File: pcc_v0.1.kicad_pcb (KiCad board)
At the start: 2 copper layers, 170.3 x 151.7 mm, 65 parts, among them J2 Conn_01x04_Socket, J3 Conn_01x02_Socket, J4 Conn_02x14_Counter_Clockwise, J6 Conn_01x04_Socket, J7 Conn_01x04_Socket, J8 Conn_01x02_Socket, K1 G9KB-1A_DC12, K2 DBR71210, K3 PCN-112D3MHZ_000, U2 4N35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

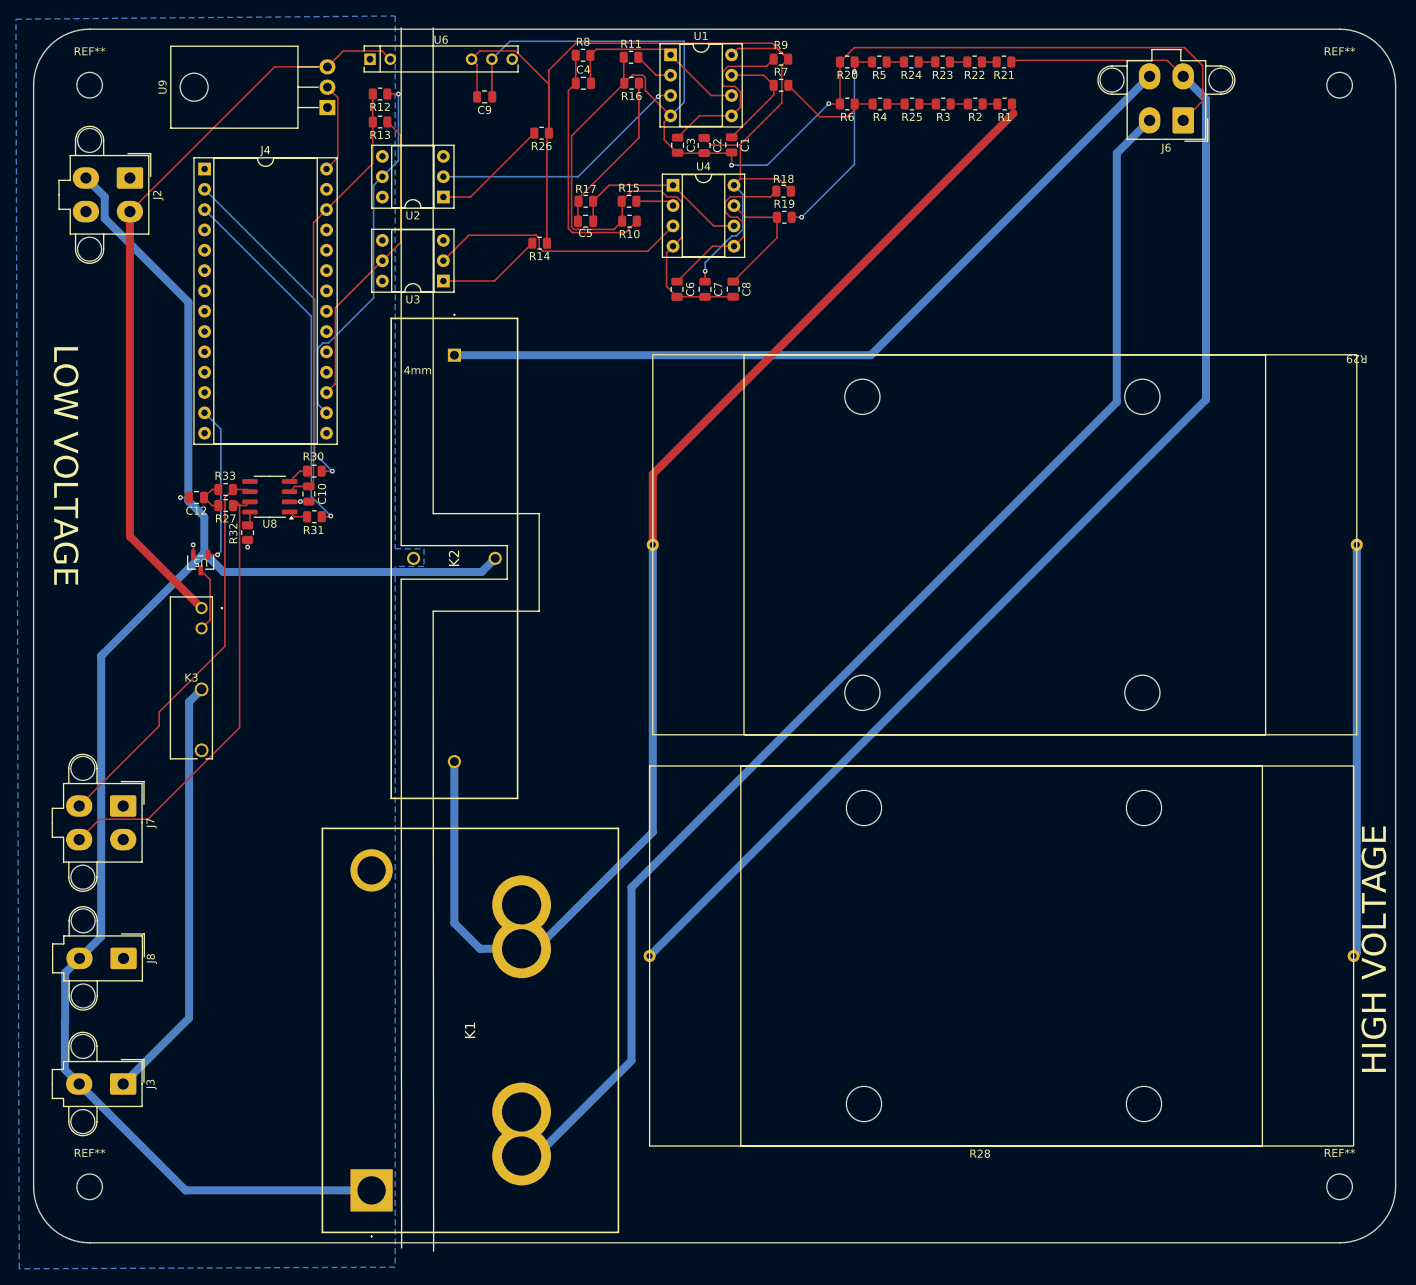
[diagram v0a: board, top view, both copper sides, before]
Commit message: made custom footprint for relay. need to measure actual size
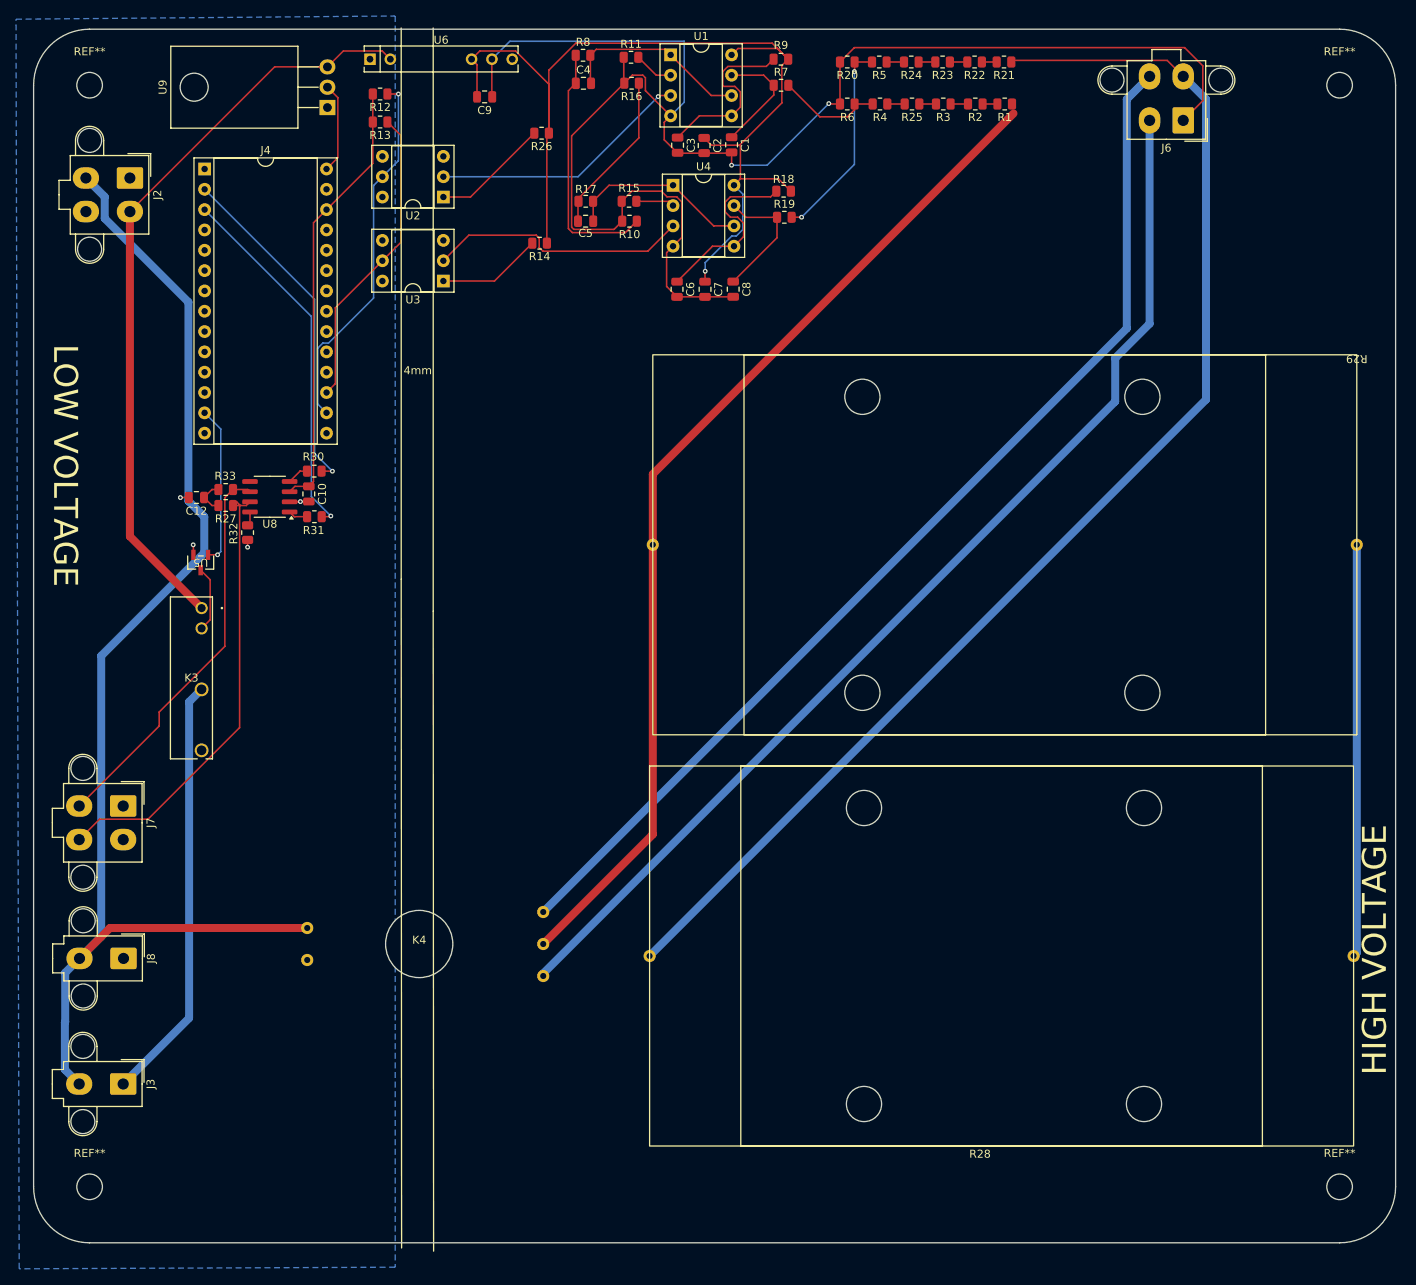
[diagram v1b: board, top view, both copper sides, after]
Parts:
- removed K1: G9KB-1A_DC12, precharge relay 2:G9KB1ADC12
- removed K2: DBR71210, discharge relay:DBR71210
- added K4: Relay_SPDT, Relay_THT:Precharge_Discharge_Relay, F.Cu at (101.0, 135.0)
- C10: value 100nF -> 100n
- C12: value 4.7nF -> 4.7n
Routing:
- net Shutdown_in: track 207.5 -> 157.4 mm
- net TS+: track 101.3 -> 135.8 mm
- net Vin_Accu: track 160.9 -> 128.2 mm
- net B+_in: track 163.0 -> 138.3 mm

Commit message: corrected relay footprint, added flyback diode
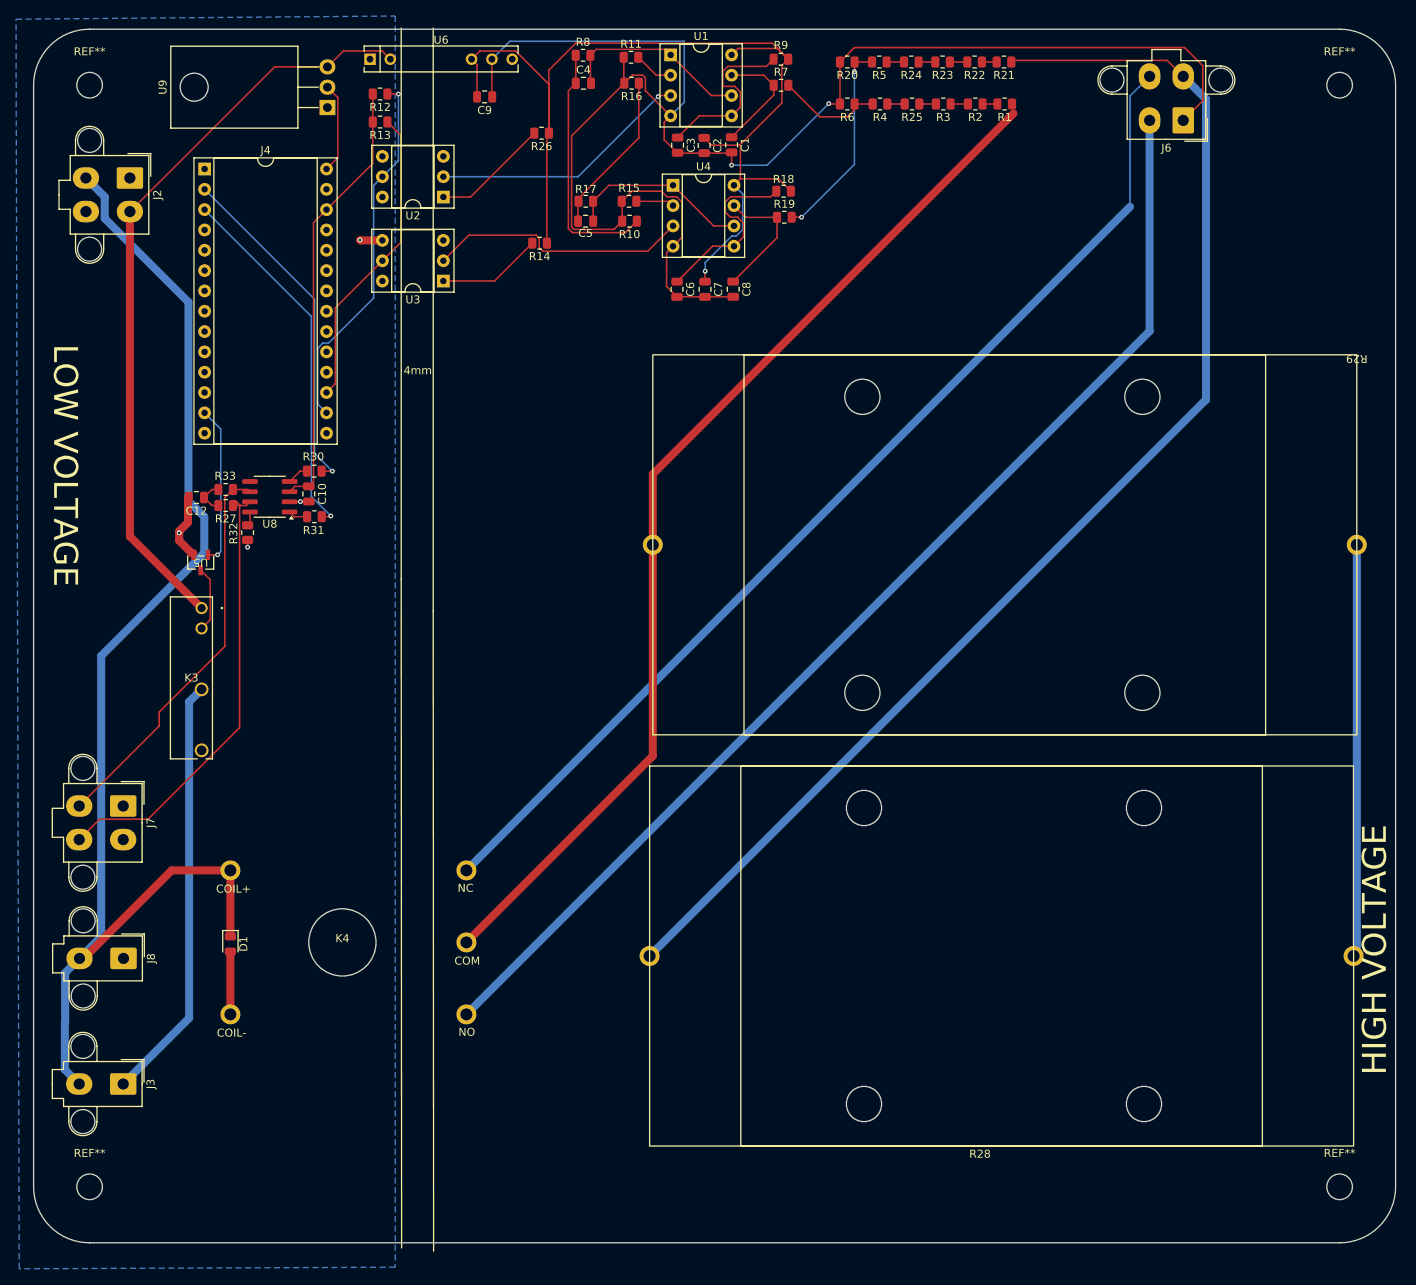
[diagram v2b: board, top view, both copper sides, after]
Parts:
- added D1: D, Diode_SMD:D_0805_2012Metric, F.Cu at (77.4, 135.0)
- moved K4 9.60 mm to (91.4, 134.8)
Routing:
- net GLV-: track 5.64 -> 22.2 mm
- net B+_in: track 138.3 -> 147.1 mm
- net Vin_Accu: track 128.2 -> 131.9 mm
- net Shutdown_in: track 157.4 -> 158.9 mm
- net TS+: track 135.8 -> 134.6 mm

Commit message: changed diode to tht and added connector labels
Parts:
- D1: footprint Diode_SMD:D_0805_2012Metric -> Diode_THT:D_5KPW_P7.62mm_Vertical_AnodeUp
- moved D1 3.80 mm to (77.4, 131.2)
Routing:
- net GLV-: track 22.2 -> 14.4 mm
- net Shutdown_in: track 158.9 -> 156.2 mm
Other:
- board text added: "CAN Bus"
- board text added: "HV IN"
- board text added: "IR+ Relay"
- board text added: "IR- Relay"
- board text added: "POWER IN"
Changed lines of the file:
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@@
 		)
 	)
-	(footprint "Diode_SMD:D_0805_2012Metric"
+	(footprint "Diode_THT:D_5KPW_P7.62mm_Vertical_AnodeUp"
 		(layer "F.Cu")
-		(at 77.4 135 -90)
-		(descr "Diode SMD 0805 (2012 Metric), square (rectangular) end terminal, IPC_7351 nominal, (Body size source: https://docs.google.com/spreadsheets/d/1BsfQQcO9C6DZCsRaXUlFlo91Tg2WpOkGARC1WS5S8t0/edit?usp=sharing), generated with kicad-footprint-generator")
-		(tags "diode")
+		(at 77.4 131.2 -90)
+		(descr "Diode, 5KPW series, Axial, Vertical, pin pitch=7.62mm, , length*diameter=9*8mm^2, , http://www.diodes.com/_files/packages/8686949.gif")
+		(tags "Diode 5KPW series Axial Vertical pin pitch 7.62mm  length 9mm diameter 8mm")
 		(property "Reference" "D1"
-			(at 0 -1.65 90)
+			(at 3.81 -5.12 -90)
 			(layer "F.SilkS")
 			(effects
@@
 		)
 		(property "Value" "D"
-			(at 0 1.65 90)
+			(at 3.81 5.12 -90)
 			(layer "F.Fab")
 			(effects
@@
 			)
 		)
-		(property "Footprint" "Diode_SMD:D_0805_2012Metric"
+		(property "Footprint" "Diode_THT:D_5KPW_P7.62mm_Vertical_AnodeUp"
 			(at 0 0 -90)
 			(unlocked yes)
@@
 		(sheetname "Root")
 		(sheetfile "pcc_v0.1.kicad_sch")
-		(attr smd)
-		(fp_line
-			(start -1.685 0.96)
-			(end 1 0.96)
-			(stroke
-				(width 0.12)
-				(type solid)
-			)
-			(layer "F.SilkS")
-		)
+		(attr through_hole)
 		(fp_line
-			(start -1.685 -0.96)
-			(end -1.685 0.96)
+			(start 4.12 0)
+			(end 5.72 0)
 			(stroke
 				(width 0.12)
@@
 			(layer "F.SilkS")
 		)
-		(fp_line
-			(start 1 -0.96)
-			(end -1.685 -0.96)
+		(fp_circle
+			(center 0 0)
+			(end 4.12 0)
 			(stroke
 				(width 0.12)
 				(type solid)
 			)
+			(fill none)
 			(layer "F.SilkS")
 		)
 		(fp_line
-			(start -1.68 0.95)
-			(end -1.68 -0.95)
+			(start -4.25 4.25)
+			(end 9.47 4.25)
 			(stroke
 				(width 0.05)
@@
 		)
 		(fp_line
-			(start 1.68 0.95)
-			(end -1.68 0.95)
+			(start 9.47 4.25)
+			(end 9.47 -4.25)
 			(stroke
 				(width 0.05)
@@
 		)
 		(fp_line
-			(start -1.68 -0.95)
-			(end 1.68 -0.95)
+			(start -4.25 -4.25)
+			(end -4.25 4.25)
 			(stroke
 				(width 0.05)
@@
 		)
 		(fp_line
-			(start 1.68 -0.95)
-			(end 1.68 0.95)
+			(start 9.47 -4.25)
+			(end -4.25 -4.25)
 			(stroke
 				(width 0.05)
@@
 		)
 		(fp_line
-			(start -1 0.6)
-			(end 1 0.6)
+			(start 0 0)
+			(end 7.62 0)
 			(stroke
 				(width 0.1)
@@
 			(layer "F.Fab")
 		)
-		(fp_line
-			(start 1 0.6)
-			(end 1 -0.6)
+		(fp_circle
+			(center 0 0)
+			(end 4 0)
 			(stroke
 				(width 0.1)
 				(type solid)
 			)
+			(fill none)
 			(layer "F.Fab")
 		)
-		(fp_line
-			(start -1 -0.3)
-			(end -1 0.6)
-			(stroke
-				(width 0.1)
-				(type solid)
+		(fp_text user "A"
+			(at 7.62 2.6 -90)
+			(layer "F.SilkS")
+			(effects
+				(font
+					(size 1 1)
+					(thickness 0.15)
+				)
 			)
-			(layer "F.Fab")
 		)
-		(fp_line
-			(start -0.7 -0.6)
-			(end -1 -0.3)
-			(stroke
-				(width 0.1)
-				(type solid)
-			)
+		(fp_text user "${REFERENCE}"
+			(at 0 -2.1 -90)
 			(layer "F.Fab")
-		)
-		(fp_line
-			(start 1 -0.6)
-			(end -0.7 -0.6)
-			(stroke
-				(width 0.1)
-				(type solid)
+			(effects
+				(font
+					(size 1 1)
+					(thickness 0.15)
+				)
 			)
-			(layer "F.Fab")
 		)
-		(fp_text user "${REFERENCE}"
-			(at 0 0 90)
+		(fp_text user "A"
+			(at 7.62 2.6 -90)
 			(layer "F.Fab")
 			(effects
 				(font
-					(size 0.5 0.5)
-					(thickness 0.08)
+					(size 1 1)
+					(thickness 0.15)
 				)
 			)
 		)
-		(pad "1" smd roundrect
-			(at -0.9375 0 270)
-			(size 0.975 1.4)
-			(layers "F.Cu" "F.Paste" "F.Mask")
-			(roundrect_rratio 0.25)
+		(pad "1" thru_hole rect
+			(at 0 0 270)
+			(size 3.2 3.2)
+			(drill 1.6)
+			(layers "*.Cu" "*.Mask")
+			(remove_unused_layers no)
 			(net 69 "Shutdown_in")
 			(pinfunction "K")
 			(pintype "passive")
 		)
-		(pad "2" smd roundrect
-			(at 0.9375 0 270)
-			(size 0.975 1.4)
-			(layers "F.Cu" "F.Paste" "F.Mask")
-			(roundrect_rratio 0.25)
+		(pad "2" thru_hole oval
+			(at 7.62 0 270)
+			(size 3.2 3.2)
+			(drill 1.6)
+			(layers "*.Cu" "*.Mask")
+			(remove_unused_layers no)
 			(net 8 "GLV-")
 			(pinfunction "A")
 			(pintype "passive")
 		)
-		(model "${KICAD8_3DMODEL_DIR}/Diode_SMD.3dshapes/D_0805_2012Metric.wrl"
+		(model "${KICAD8_3DMODEL_DIR}/Diode_THT.3dshapes/D_5KPW_P7.62mm_Vertical_AnodeUp.wrl"
 			(offset
 				(xyz 0 0 0)
@@
 	)
 	(gr_line
-		(start 98.773804 129.199896)
-		(end 98.8 173)
-		(stroke
-			(width 0.1)
-			(type default)
-		)
-		(layer "F.SilkS")
-	)
-	(gr_line
 		(start 98.772608 127.200016)
 		(end 98.773804 129.199896)
@@
 		(layer "F.SilkS")
 	)
+	(gr_line
+		(start 98.773804 129.199896)
+		(end 98.8 173)
+		(stroke
+			(width 0.1)
+			(type default)
+		)
+		(layer "F.SilkS")
+	)
 	(gr_arc
 		(start 59.800253 172.350253)
@@
 		(layer "Edge.Cuts")
 	)
+	(gr_text "CAN Bus"
+		(at 70.2 125 90)
+		(layer "F.SilkS")
+		(effects
+			(font
+				(size 1.5 1.5)
+				(thickness 0.3)
+				(bold yes)
+			)
+			(justify left bottom)
+		)
+	)
+	(gr_text "HV IN"
+		(at 191.2 39 0)
+		(layer "F.SilkS")
+		(effects
+			(font
+				(size 1.5 1.5)
+				(thickness 0.3)
+				(bold yes)
+			)
+			(justify left bottom)
+		)
+	)
 	(gr_text "4mm"
 		(at 99.050253 63.900253 0)
@@
 		)
 	)
+	(gr_text "POWER IN"
+		(at 71.2 46.8 90)
+		(layer "F.SilkS")
+		(effects
+			(font
+				(size 1.5 1.5)
+				(thickness 0.3)
+				(bold yes)
+			)
+			(justify left bottom)
+		)
+	)
+	(gr_text "IR- Relay"
+		(at 70.2 142.4 90)
+		(layer "F.SilkS")
+		(effects
+			(font
+				(size 1.5 1.5)
+				(thickness 0.3)
+				(bold yes)
+			)
+			(justify left bottom)
+		)
+	)
 	(gr_text "HIGH VOLTAGE\n"
 		(at 222.2 151.4 90)
@@
 		)
 	)
+	(gr_text "IR+ Relay"
+		(at 70.6 158 90)
+		(layer "F.SilkS")
+		(effects
+			(font
+				(size 1.5 1.5)
+				(thickness 0.3)
+				(bold yes)
+			)
+			(justify left bottom)
+		)
+	)
 	(gr_text "${REFERENCE}"
 		(at 146.6425 40.66 0)
@@
 	)
 	(segment
-		(start 77.4 143.8)
-		(end 77.4 136.05)
-		(width 1)
-		(layer "F.Cu")
-		(net 8)
-	)
-	(segment
 		(start 93.650253 47.050253)
 		(end 93.6 47)
@@
 	(segment
 		(start 77.4 125.8)
-		(end 77.4 133.95)
-		(width 1)
-		(layer "F.Cu")
-		(net 69)
-	)
-	(segment
-		(start 77.4 125.8)
 		(end 70.058198 125.8)
 		(width 1)
@@
 		(width 1)
 		(layer "F.Cu")
+		(net 69)
+	)
+	(segment
+		(start 77.4 131.2)
+		(end 77.4 125.8)
+		(width 1)
+		(layer "F.Cu")
